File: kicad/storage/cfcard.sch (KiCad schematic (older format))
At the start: 2 parts, among them J2 Conn_02x20_Odd_Even, J3 Conn_01x02

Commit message: Finish storage card
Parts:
- added C4: C, Capacitor_THT:C_Disc_D6.0mm_W2.5mm_P5.00mm, symbol Device:C
- J2: footprint Connector_PinHeader_2.54mm:PinHeader_2x20_P2.54mm_Vertical -> storage:cfcard
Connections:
- net GND: now also C4.2
- net VCC: now also C4.1
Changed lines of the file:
@@
 $Descr A4 11693 8268
 encoding utf-8
-Sheet 3 3
+Sheet 2 3
 Title ""
 Date ""
@@
 F 0 "J4" H 4800 4317 50  0000 C CNN
 F 1 "Conn_02x20_Odd_Even" H 4800 4226 50  0000 C CNN
-F 2 "Connector_PinHeader_2.54mm:PinHeader_2x20_P2.54mm_Vertical" H 4750 3200 50  0001 C CNN
+F 2 "storage:cfcard" H 4750 3200 50  0001 C CNN
 F 3 "~" H 4750 3200 50  0001 C CNN
 	1    4750 3200
@@
 Text GLabel 6350 2450 0    50   Input ~ 0
 GND
+$Comp
+L Device:C C4
+U 1 1 60C47AAF
+P 6350 3200
+AR Path="/60BC0128/60C47AAF" Ref="C4"  Part="1"
+AR Path="/60BC913C/60C47AAF" Ref="C5"  Part="1"
+F 0 "C5" H 6465 3246 50  0000 L CNN
+F 1 "C" H 6465 3155 50  0000 L CNN
+F 2 "Capacitor_THT:C_Disc_D6.0mm_W2.5mm_P5.00mm" H 6388 3050 50  0001 C CNN
+F 3 "~" H 6350 3200 50  0001 C CNN
+	1    6350 3200
+	1    0    0    -1
+$EndComp
+Text GLabel 6350 3050 2    50   Input ~ 0
+VCC
+Text GLabel 6350 3350 2    50   Input ~ 0
+GND
 $EndSCHEMATC

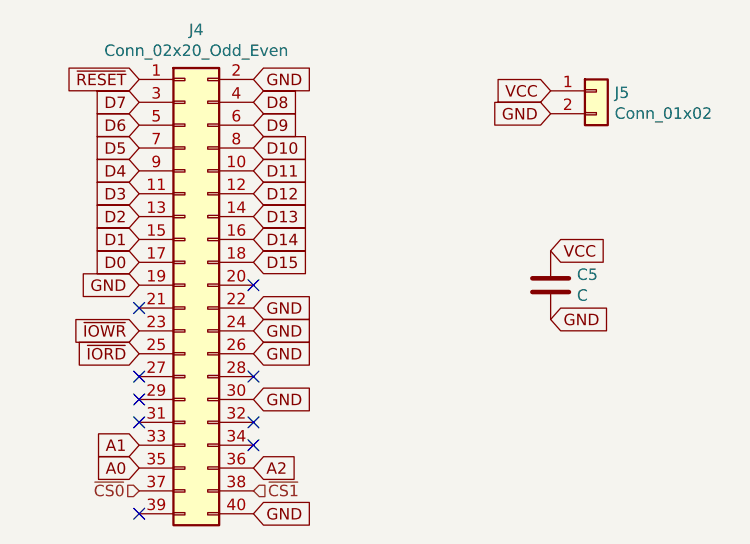
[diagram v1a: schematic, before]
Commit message: Add 74HCT245 bus transceivers to storage card
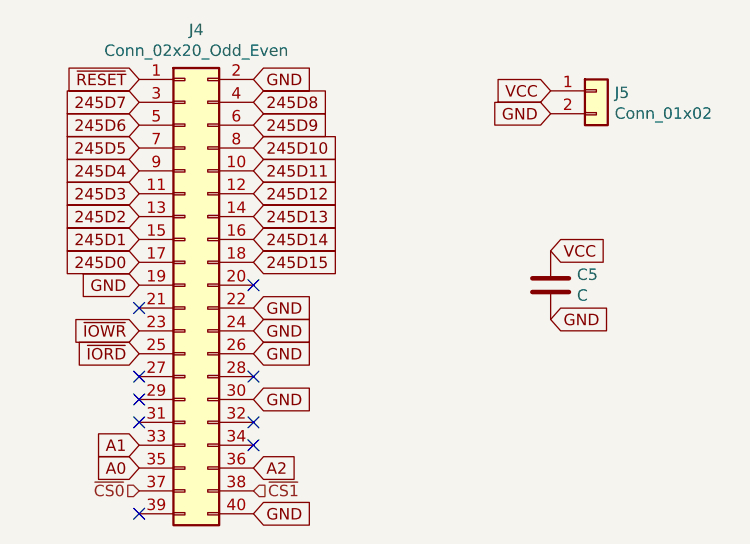
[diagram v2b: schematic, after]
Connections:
- net D0 renamed 245D0
- net D1 renamed 245D1
- net D10 renamed 245D10
- net D11 renamed 245D11
- net D12 renamed 245D12
- net D13 renamed 245D13
- net D14 renamed 245D14
- net D15 renamed 245D15
- net D2 renamed 245D2
- net D3 renamed 245D3
- net D4 renamed 245D4
- net D5 renamed 245D5
- net D6 renamed 245D6
- net D7 renamed 245D7
- net D8 renamed 245D8
- net D9 renamed 245D9
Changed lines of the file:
@@
 $Descr A4 11693 8268
 encoding utf-8
-Sheet 2 3
+Sheet 3 3
 Title ""
 Date ""
@@
 GND
 Text GLabel 4550 2400 0    50   Input ~ 0
-D7
+245D7
 Text GLabel 4550 2500 0    50   Input ~ 0
-D6
+245D6
 Text GLabel 4550 2600 0    50   Input ~ 0
-D5
+245D5
 Text GLabel 4550 2700 0    50   Input ~ 0
-D4
+245D4
 Text GLabel 4550 2800 0    50   Input ~ 0
-D3
+245D3
 Text GLabel 4550 2900 0    50   Input ~ 0
-D2
+245D2
 Text GLabel 4550 3000 0    50   Input ~ 0
-D1
+245D1
 Text GLabel 4550 3100 0    50   Input ~ 0
-D0
+245D0
 Text GLabel 5050 2400 2    50   Input ~ 0
-D8
+245D8
 Text GLabel 5050 2500 2    50   Input ~ 0
-D9
+245D9
 Text GLabel 5050 2600 2    50   Input ~ 0
-D10
+245D10
 Text GLabel 5050 2700 2    50   Input ~ 0
-D11
+245D11
 Text GLabel 5050 2800 2    50   Input ~ 0
-D12
+245D12
 Text GLabel 5050 2900 2    50   Input ~ 0
-D13
+245D13
 Text GLabel 5050 3000 2    50   Input ~ 0
-D14
+245D14
 Text GLabel 5050 3100 2    50   Input ~ 0
-D15
+245D15
 Text GLabel 4550 3200 0    50   Input ~ 0
 GND
